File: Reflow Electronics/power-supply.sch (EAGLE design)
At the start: 19 parts, among them IC1 LM2574N-5.0

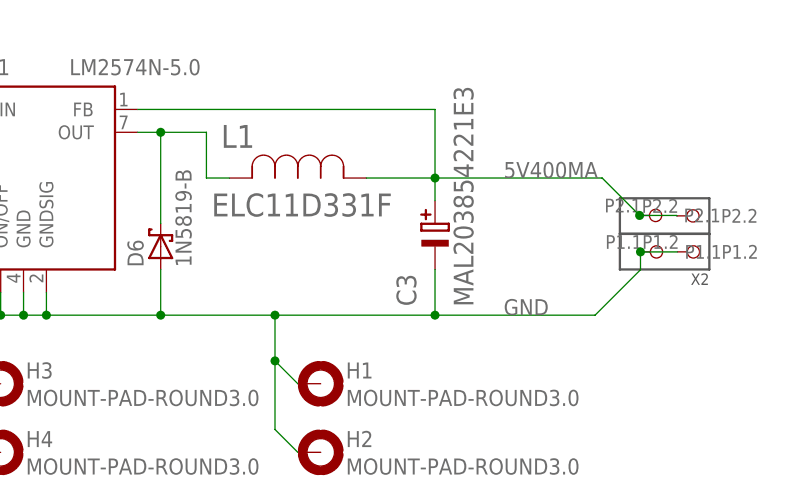
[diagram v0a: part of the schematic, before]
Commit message: power supply electronics
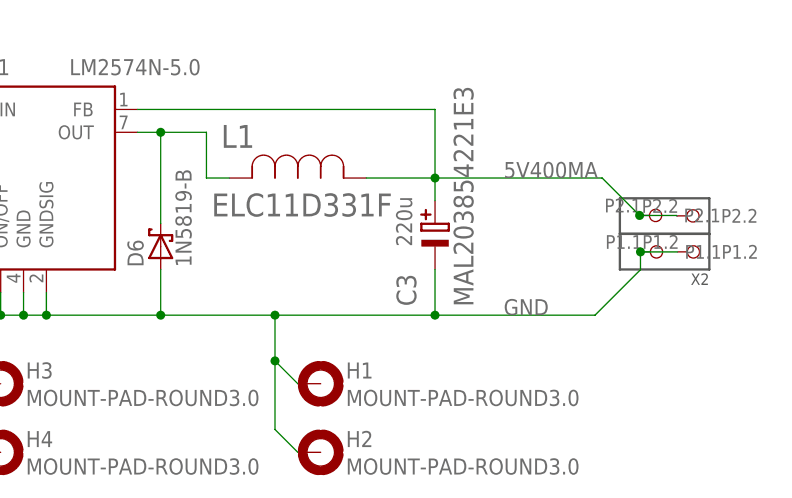
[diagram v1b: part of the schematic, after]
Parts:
- C3: CAPACITANCE (none) -> 220u
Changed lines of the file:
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@@
 <grid distance="0.1" unitdist="inch" unit="inch" style="lines" multiple="1" display="no" altdistance="0.01" altunitdist="inch" altunit="inch"/>
 <layers>
-<layer number="1" name="Top" color="4" fill="1" visible="no" active="no"/>
-<layer number="16" name="Bottom" color="1" fill="1" visible="no" active="no"/>
-<layer number="17" name="Pads" color="2" fill="1" visible="no" active="no"/>
-<layer number="18" name="Vias" color="2" fill="1" visible="no" active="no"/>
-<layer number="19" name="Unrouted" color="6" fill="1" visible="no" active="no"/>
-<layer number="20" name="Dimension" color="15" fill="1" visible="no" active="no"/>
-<layer number="21" name="tPlace" color="7" fill="1" visible="no" active="no"/>
-<layer number="22" name="bPlace" color="7" fill="1" visible="no" active="no"/>
-<layer number="23" name="tOrigins" color="15" fill="1" visible="no" active="no"/>
-<layer number="24" name="bOrigins" color="15" fill="1" visible="no" active="no"/>
-<layer number="25" name="tNames" color="7" fill="1" visible="no" active="no"/>
-<layer number="26" name="bNames" color="7" fill="1" visible="no" active="no"/>
-<layer number="27" name="tValues" color="7" fill="1" visible="no" active="no"/>
-<layer number="28" name="bValues" color="7" fill="1" visible="no" active="no"/>
+<layer number="1" name="Top" color="4" fill="1" visible="yes" active="no"/>
+<layer number="16" name="Bottom" color="1" fill="1" visible="yes" active="no"/>
+<layer number="17" name="Pads" color="2" fill="1" visible="yes" active="no"/>
+<layer number="18" name="Vias" color="2" fill="1" visible="yes" active="no"/>
+<layer number="19" name="Unrouted" color="6" fill="1" visible="yes" active="no"/>
+<layer number="20" name="Dimension" color="24" fill="1" visible="yes" active="no"/>
+<layer number="21" name="tPlace" color="7" fill="1" visible="yes" active="no"/>
+<layer number="22" name="bPlace" color="7" fill="1" visible="yes" active="no"/>
+<layer number="23" name="tOrigins" color="15" fill="1" visible="yes" active="no"/>
+<layer number="24" name="bOrigins" color="15" fill="1" visible="yes" active="no"/>
+<layer number="25" name="tNames" color="7" fill="1" visible="yes" active="no"/>
+<layer number="26" name="bNames" color="7" fill="1" visible="yes" active="no"/>
+<layer number="27" name="tValues" color="7" fill="1" visible="yes" active="no"/>
+<layer number="28" name="bValues" color="7" fill="1" visible="yes" active="no"/>
 <layer number="29" name="tStop" color="7" fill="3" visible="no" active="no"/>
 <layer number="30" name="bStop" color="7" fill="6" visible="no" active="no"/>
@@
 <layer number="35" name="tGlue" color="7" fill="4" visible="no" active="no"/>
 <layer number="36" name="bGlue" color="7" fill="5" visible="no" active="no"/>
-<layer number="37" name="tTest" color="7" fill="1" visible="no" active="no"/>
-<layer number="38" name="bTest" color="7" fill="1" visible="no" active="no"/>
+<layer number="37" name="tTest" color="7" fill="1" visible="yes" active="no"/>
+<layer number="38" name="bTest" color="7" fill="1" visible="yes" active="no"/>
 <layer number="39" name="tKeepout" color="4" fill="11" visible="no" active="no"/>
 <layer number="40" name="bKeepout" color="1" fill="11" visible="no" active="no"/>
@@
 <layer number="44" name="Drills" color="7" fill="1" visible="no" active="no"/>
 <layer number="45" name="Holes" color="7" fill="1" visible="no" active="no"/>
-<layer number="46" name="Milling" color="3" fill="1" visible="no" active="no"/>
-<layer number="47" name="Measures" color="7" fill="1" visible="no" active="no"/>
-<layer number="48" name="Document" color="7" fill="1" visible="no" active="no"/>
-<layer number="49" name="Reference" color="7" fill="1" visible="no" active="no"/>
-<layer number="51" name="tDocu" color="7" fill="1" visible="no" active="no"/>
-<layer number="52" name="bDocu" color="7" fill="1" visible="no" active="no"/>
+<layer number="46" name="Milling" color="3" fill="1" visible="yes" active="no"/>
+<layer number="47" name="Measures" color="7" fill="1" visible="yes" active="no"/>
+<layer number="48" name="Document" color="7" fill="1" visible="yes" active="no"/>
+<layer number="49" name="Reference" color="7" fill="1" visible="yes" active="no"/>
+<layer number="51" name="tDocu" color="7" fill="1" visible="yes" active="no"/>
+<layer number="52" name="bDocu" color="7" fill="1" visible="yes" active="no"/>
 <layer number="88" name="SimResults" color="9" fill="1" visible="yes" active="yes"/>
 <layer number="89" name="SimProbes" color="9" fill="1" visible="yes" active="yes"/>
@@
 <part name="L1" library="reflow-oven" deviceset="ELC11D331F" device=""/>
 <part name="D6" library="diode" library_urn="urn:adsk.eagle:library:210" deviceset="1N581*" device="" package3d_urn="urn:adsk.eagle:package:43421/1" technology="9-B"/>
-<part name="C3" library="reflow-oven" deviceset="MAL203854221E3" device=""/>
+<part name="C3" library="reflow-oven" deviceset="MAL203854221E3" device="">
+<attribute name="CAPACITANCE" value="220u"/>
+</part>
 <part name="X1" library="con-wago_2604" deviceset="2604-1102" device=""/>
 <part name="X2" library="con-wago_2604" deviceset="2604-1102" device=""/>
@@
 <instance part="L1" gate="A" x="119.38" y="60.96"/>
 <instance part="D6" gate="G$1" x="111.76" y="53.34" rot="R90"/>
-<instance part="C3" gate="A" x="142.24" y="50.8" rot="R90"/>
+<instance part="C3" gate="A" x="142.24" y="50.8" rot="R90">
+<attribute name="CAPACITANCE" x="139.7" y="53.34" size="1.778" layer="96" rot="R90"/>
+</instance>
 <instance part="X1" gate="G$1" x="-43.18" y="71.12"/>
 <instance part="X2" gate="G$1" x="172.72" y="50.8" rot="R180"/>

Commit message: Fixed schematic and board for problems found on first iteration
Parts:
- C3: value MAL203854221E3 -> 220u; device reflow-oven:MAL203854221E3 -> rcl:CPOL-EUE2-5; CAPACITANCE 220u -> (none)
- L1: value ELC11D331F -> 330UH; device reflow-oven:ELC11D331F -> Panasonic-ELC:ELC11D331F-11D
- TR1: value (none) -> 44231
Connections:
- net 5V400MA: now also C3.+; no longer C3.22
- net GND: now also C3.-; no longer C3.11
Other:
- moved on the sheet: L1

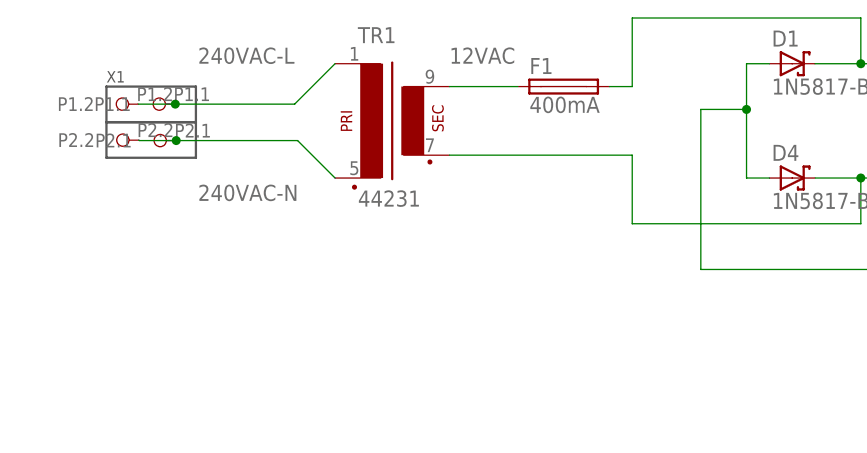
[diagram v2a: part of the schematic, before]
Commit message: Tweaked power supply for future following testing. Added BOM.
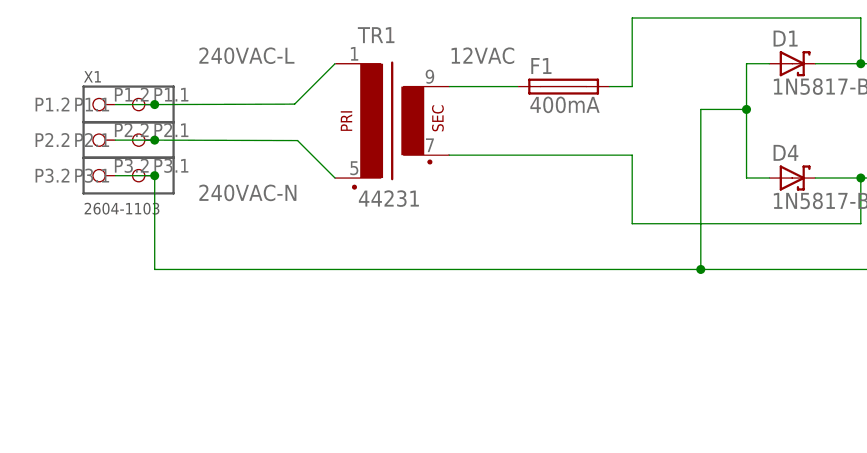
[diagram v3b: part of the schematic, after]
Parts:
- X1: value (none) -> 2604-1103; device con-wago_2604:2604-1102 -> con-wago_2604:2604-1103
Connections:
- net GND: now also X1.P3.1, X1.P3.2
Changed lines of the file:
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@@
 <part name="L1" library="Panasonic-ELC" deviceset="ELC" device="-11D" technology="11D331F" value=" 330UH "/>
 <part name="D6" library="diode" library_urn="urn:adsk.eagle:library:210" deviceset="1N581*" device="" package3d_urn="urn:adsk.eagle:package:43421/1" technology="9-B"/>
-<part name="X1" library="con-wago_2604" deviceset="2604-1102" device=""/>
+<part name="X1" library="con-wago_2604" deviceset="2604-1103" device=""/>
 <part name="X2" library="con-wago_2604" deviceset="2604-1102" device=""/>
 <part name="H1" library="holes" library_urn="urn:adsk.eagle:library:237" deviceset="MOUNT-PAD-ROUND" device="3.0" package3d_urn="urn:adsk.eagle:package:14280/1"/>
@@
 <instance part="L1" gate="A" x="121.92" y="60.96"/>
 <instance part="D6" gate="G$1" x="111.76" y="53.34" rot="R90"/>
-<instance part="X1" gate="G$1" x="-43.18" y="71.12"/>
+<instance part="X1" gate="G$1" x="-45.72" y="71.12"/>
 <instance part="X2" gate="G$1" x="172.72" y="50.8" rot="R180"/>
 <instance part="H1" gate="G$1" x="129.54" y="38.1"/>
@@
 <wire x1="142.24" y1="50.8" x2="142.24" y2="45.72" width="0.1524" layer="91"/>
 <junction x="142.24" y="45.72"/>
+<pinref part="X1" gate="G$1" pin="P3.2"/>
+<pinref part="X1" gate="G$1" pin="P3.1"/>
+<wire x1="-42.22" y1="61.22" x2="-37.82" y2="61.22" width="0.1524" layer="91"/>
+<wire x1="-37.82" y1="61.22" x2="-37.82" y2="50.8" width="0.1524" layer="91"/>
+<wire x1="-37.82" y1="50.8" x2="22.86" y2="50.8" width="0.1524" layer="91"/>
+<junction x="-37.82" y="61.22"/>
+<junction x="22.86" y="50.8"/>
 </segment>
 </net>
@@
 <pinref part="X1" gate="G$1" pin="P1.1"/>
 <wire x1="-17.78" y1="73.66" x2="-22.27" y2="69.17" width="0.1524" layer="91"/>
-<wire x1="-22.27" y1="69.17" x2="-35.53" y2="69.17" width="0.1524" layer="91"/>
+<wire x1="-22.27" y1="69.17" x2="-37.82" y2="69.12" width="0.1524" layer="91"/>
 <pinref part="X1" gate="G$1" pin="P1.2"/>
-<wire x1="-35.53" y1="69.17" x2="-39.63" y2="69.17" width="0.1524" layer="91"/>
-<junction x="-35.53" y="69.17"/>
+<wire x1="-37.82" y1="69.12" x2="-42.22" y2="69.12" width="0.1524" layer="91"/>
+<junction x="-37.82" y="69.12"/>
 <label x="-33.02" y="73.66" size="1.778" layer="95"/>
 </segment>
@@
 <pinref part="X1" gate="G$1" pin="P2.1"/>
 <wire x1="-17.78" y1="60.96" x2="-21.94" y2="65.12" width="0.1524" layer="91"/>
-<wire x1="-21.94" y1="65.12" x2="-35.43" y2="65.12" width="0.1524" layer="91"/>
+<wire x1="-21.94" y1="65.12" x2="-37.82" y2="65.17" width="0.1524" layer="91"/>
+<label x="-33.02" y="58.42" size="1.778" layer="95"/>
 <pinref part="X1" gate="G$1" pin="P2.2"/>
-<wire x1="-35.43" y1="65.12" x2="-39.53" y2="65.12" width="0.1524" layer="91"/>
-<wire x1="-39.53" y1="65.12" x2="-39.58" y2="65.17" width="0.1524" layer="91"/>
-<junction x="-35.43" y="65.12"/>
-<label x="-33.02" y="58.42" size="1.778" layer="95"/>
-</segment>
-</net>
+<wire x1="-42.22" y1="65.17" x2="-37.82" y2="65.17" width="0.1524" layer="91"/>
+<junction x="-37.82" y="65.17"/>
+</segment>
+</net>
